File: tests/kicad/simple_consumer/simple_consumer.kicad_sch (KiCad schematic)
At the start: 8 parts

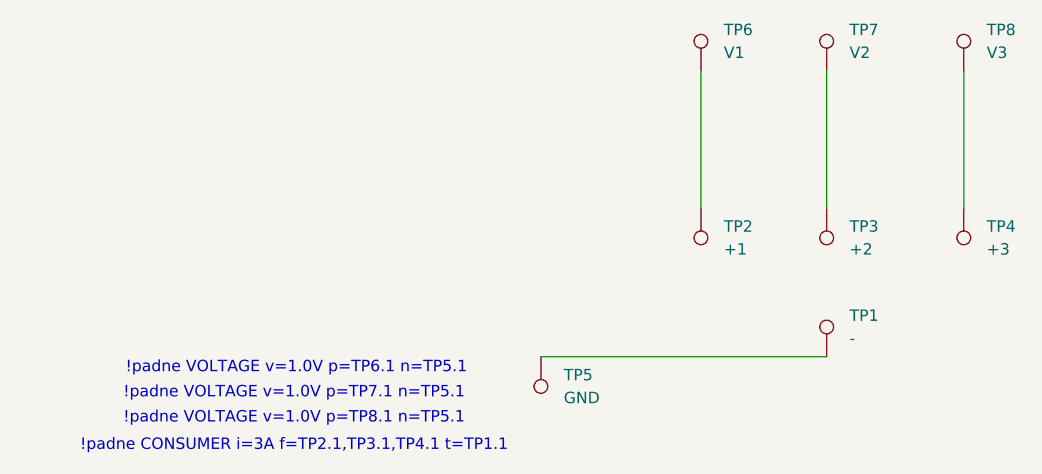
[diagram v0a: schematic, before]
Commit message: refactor(kicad): Port everything else to the new BaseLumpedSpec API
There are still some weird loose ends, such as requiring force_coupling
on the VoltageRegulator, but that is a bug to be solved on another day.
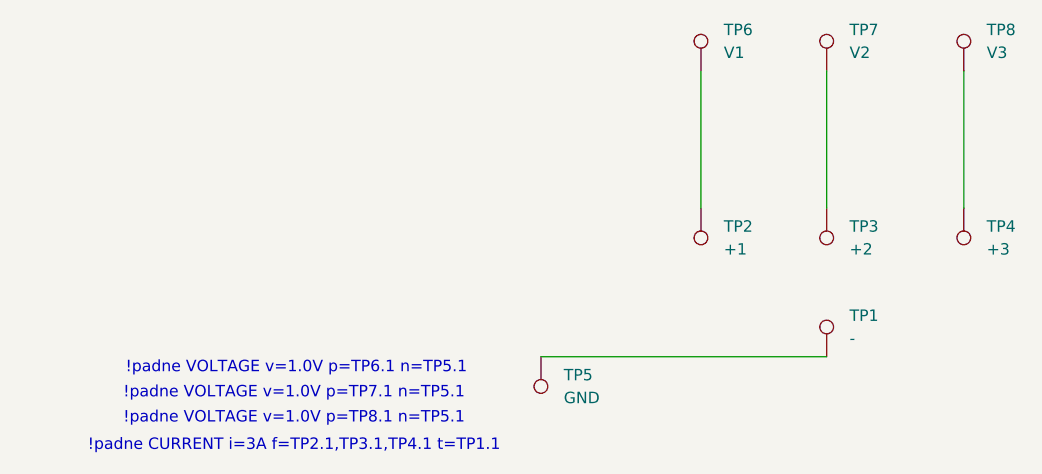
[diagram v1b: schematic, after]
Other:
- note added: "!padne CURRENT i=3A f=TP2.1,TP3.1,TP4.1 t=TP1.1"
- note removed: "!padne CONSUMER i=3A f=TP2.1,TP3.1,TP4.1 t=TP1.1"
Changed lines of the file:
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@@
 		)
 	)
-	(text "!padne CONSUMER i=3A f=TP2.1,TP3.1,TP4.1 t=TP1.1"
+	(text "!padne CURRENT i=3A f=TP2.1,TP3.1,TP4.1 t=TP1.1"
 		(exclude_from_sim no)
 		(at 72.898 103.886 0)
